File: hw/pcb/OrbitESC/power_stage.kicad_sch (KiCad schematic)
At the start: 0 parts

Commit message: Add power stage components
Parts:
- added C12, C13, C15, C17: 100nF, Capacitor_SMD:C_0402_1005Metric, symbol Device:C
- added C14, C16, C19, C20, C21: 2.2uF, Capacitor_SMD:C_0805_2012Metric, symbol Device:C
- added C18: 10uF, Capacitor_SMD:C_0805_2012Metric, symbol Device:C
- added R21, R22, R23, R25, R28, R29, R30, R31, R34: 10k, Resistor_SMD:R_0402_1005Metric, symbol Device:R_US
- added R24: 1.5k, Resistor_SMD:R_0402_1005Metric, symbol Device:R_US
- added R26, R27, R32, R33, R35, R36: 1k, Resistor_SMD:R_0402_1005Metric, symbol Device:R_US
- added U5: DRV8300DRGER, Package_DFN_QFN:VQFN-24-1EP_4x4mm_P0.5mm_EP2.45x2.45mm_ThermalVias, symbol GateDrivers:DRV8300DRGER
- added U6: TSV994, Package_SO:TSSOP-14_4.4x5mm_P0.65mm, symbol Amplifier_Operational:TSV994
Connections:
- new net: R25.2, R26.2, U6.2 (-)
- new net: R21.1, R22.2, U6.12 (+)
- new net: C21.1, U5.14 (BSTC)
- new net: C20.1, U5.17 (BSTB)
- new net: C19.1, U5.20 (BSTA)
- new net: C14.1, R28.1, U6.13 (-), U6.14
- new net: R33.2, U6.10 (+)
- new net: R31.2, R32.2, U6.9 (-)
- new net: R27.2, U6.3 (+)
- new net: R34.2, R35.2, U6.6 (-)
- new net: R36.2, U6.5 (+)
- new net +3.3V: R29.2
- new net +3.3VADC: C12.2, C16.1, R21.2, U6.4 (V+)
- new net AH: U5.22 (INHA)
- new net AL: U5.1 (INLA)
- new net A_ISENSE_N: R36.1
- new net A_ISENSE_P: R35.1
- new net BH: U5.23 (INHB)
- new net BL: U5.2 (INLB)
- new net B_ISENSE_N: R33.1
- new net B_ISENSE_P: R32.1
- new net CH: U5.24 (INHC)
- new net CL: U5.3 (INLC)
- new net C_ISENSE_N: R27.1
- new net C_ISENSE_P: R26.1
- new net GHA: U5.19 (GHA)
- new net GHB: U5.16 (GHB)
- new net GHC: U5.13 (GHC)
- new net GLA: U5.11 (GLA)
- new net GLB: U5.10 (GLB)
- new net GLC: U5.9 (GLC)
- new net GND: C12.1, C14.2, C16.2, C17.1, C18.2, R22.1, U5.6 (GND), U6.11 (V-)
- new net GNDD: C13.2, C15.2, R24.2, R30.1
- new net IA: R34.1, U6.7
- new net IB: R31.1, U6.8
- new net IC: R25.1, U6.1
- new net ISenseVRef: R28.2
- new net SHA: C19.2, U5.18 (SHA)
- new net SHB: C20.2, U5.15 (SHB)
- new net SHC: C21.2, U5.12 (SHC)
- new net VDC: C17.2, C18.1, R23.2, U5.4 (GVDD)
- new net VL: C15.1, R29.1, R30.2
- new net VS: C13.1, R23.1, R24.1
- no-connect marks 0 -> 2
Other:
- note added: "3PH Drive Temp Sense"
- note added: "Logic Voltage Sense"
- note added: "Motor Terminal Voltage"
- note added: "Supply Voltage Sense"

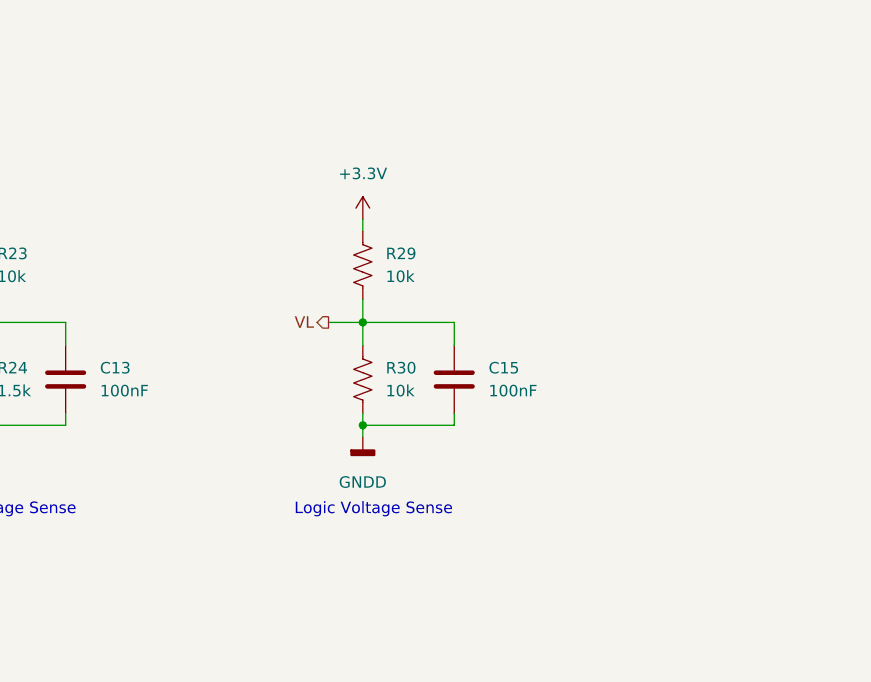
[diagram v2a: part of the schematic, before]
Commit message: Fill out majority of schematic
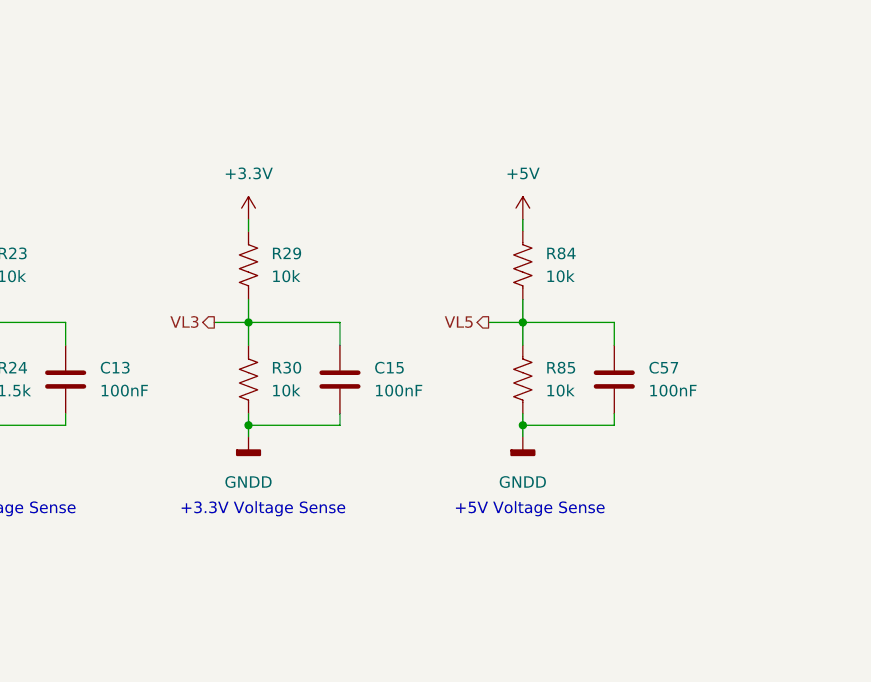
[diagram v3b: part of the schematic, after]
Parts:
- added C57: 100nF, Capacitor_SMD:C_0402_1005Metric, symbol Device:C
- added R84, R85: 10k, Resistor_SMD:R_0402_1005Metric, symbol Device:R_US
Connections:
- net GNDD: now also C57.2, R85.1
- net VL renamed VL3
- new net +5V: R84.2
- new net VL5: C57.1, R84.1, R85.2
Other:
- note added: "+3.3V Voltage Sense"
- note added: "+5V Voltage Sense"
- note removed: "Logic Voltage Sense"
- moved on the sheet: C15, R29, R30

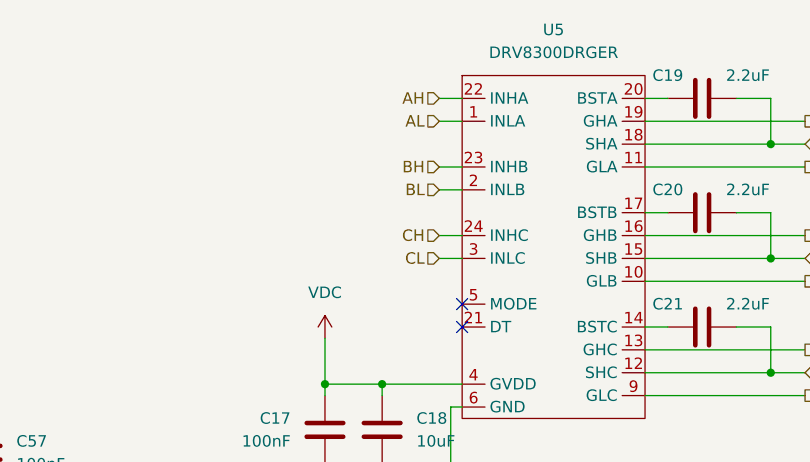
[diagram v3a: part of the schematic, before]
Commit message: Add test pads
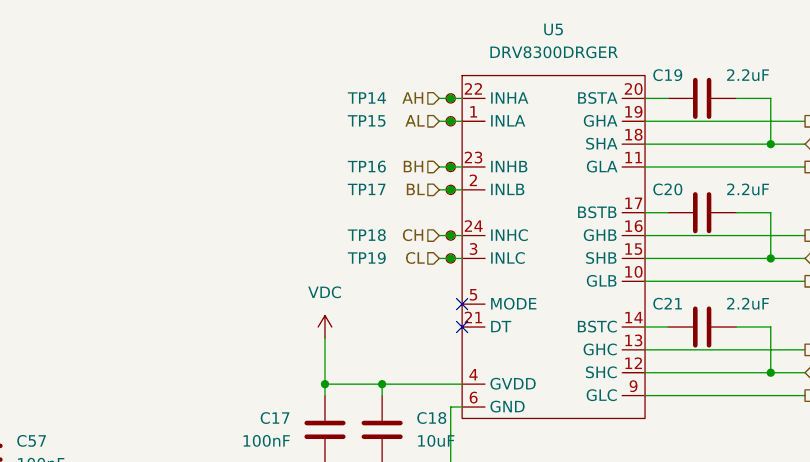
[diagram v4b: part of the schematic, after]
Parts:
- added TP14: AH, TestPoint:TestPoint_Pad_D1.0mm, symbol Connector:TestPoint_Small
- added TP15: AL, TestPoint:TestPoint_Pad_D1.0mm, symbol Connector:TestPoint_Small
- added TP16: BH, TestPoint:TestPoint_Pad_D1.0mm, symbol Connector:TestPoint_Small
- added TP17: BL, TestPoint:TestPoint_Pad_D1.0mm, symbol Connector:TestPoint_Small
- added TP18: CH, TestPoint:TestPoint_Pad_D1.0mm, symbol Connector:TestPoint_Small
- added TP19: CL, TestPoint:TestPoint_Pad_D1.0mm, symbol Connector:TestPoint_Small
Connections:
- net AH: now also TP14.1
- net AL: now also TP15.1
- net BH: now also TP16.1
- net BL: now also TP17.1
- net CH: now also TP18.1
- net CL: now also TP19.1
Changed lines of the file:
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@@
   (junction (at 236.22 48.26) (diameter 0) (color 0 0 0 0)
   )
+  (junction (at 200.66 45.72) (diameter 0) (color 0 0 0 0)
+  )
   (junction (at 151.13 138.43) (diameter 0) (color 0 0 0 0)
   )
+  (junction (at 200.66 58.42) (diameter 0) (color 0 0 0 0)
+  )
   (junction (at 236.22 73.66) (diameter 0) (color 0 0 0 0)
   )
@@
   (junction (at 236.22 60.96) (diameter 0) (color 0 0 0 0)
   )
+  (junction (at 200.66 60.96) (diameter 0) (color 0 0 0 0)
+  )
   (junction (at 134.62 165.186) (diameter 0) (color 0 0 0 0)
   )
@@
   (junction (at 77.47 76.2) (diameter 0) (color 0 0 0 0)
   )
+  (junction (at 200.66 43.18) (diameter 0) (color 0 0 0 0)
+  )
   (junction (at 196.85 140.97) (diameter 0) (color 0 0 0 0)
   )
   (junction (at 186.69 74.93) (diameter 0) (color 0 0 0 0)
+  )
+  (junction (at 200.66 53.34) (diameter 0) (color 0 0 0 0)
+  )
+  (junction (at 200.66 50.8) (diameter 0) (color 0 0 0 0)
   )
   (junction (at 107.95 87.63) (diameter 0) (color 0 0 0 0)
@@
   (no_connect (at 201.93 66.04))
   (no_connect (at 201.93 68.58))
-  (wire (pts (xy 199.39 50.8) (xy 201.93 50.8))
+  (wire (pts (xy 199.39 50.8) (xy 200.66 50.8))
     (stroke (width 0) (type default) (color 0 0 0 0))
   )
@@
     (stroke (width 0) (type default) (color 0 0 0 0))
   )
+  (wire (pts (xy 200.66 58.42) (xy 201.93 58.42))
+    (stroke (width 0) (type default) (color 0 0 0 0))
+  )
   (wire (pts (xy 186.69 74.93) (xy 186.69 76.2))
     (stroke (width 0) (type default) (color 0 0 0 0))
   )
-  (wire (pts (xy 199.39 45.72) (xy 201.93 45.72))
+  (wire (pts (xy 199.39 45.72) (xy 200.66 45.72))
+    (stroke (width 0) (type default) (color 0 0 0 0))
+  )
+  (wire (pts (xy 200.66 50.8) (xy 201.93 50.8))
     (stroke (width 0) (type default) (color 0 0 0 0))
   )
@@
     (stroke (width 0) (type default) (color 0 0 0 0))
   )
+  (wire (pts (xy 200.66 45.72) (xy 201.93 45.72))
+    (stroke (width 0) (type default) (color 0 0 0 0))
+  )
   (wire (pts (xy 236.22 73.66) (xy 240.03 73.66))
     (stroke (width 0) (type default) (color 0 0 0 0))
@@
     (stroke (width 0) (type default) (color 0 0 0 0))
   )
+  (wire (pts (xy 200.66 43.18) (xy 201.93 43.18))
+    (stroke (width 0) (type default) (color 0 0 0 0))
+  )
   (wire (pts (xy 86.36 174.076) (xy 88.9 174.076))
     (stroke (width 0) (type default) (color 0 0 0 0))
@@
     (stroke (width 0) (type default) (color 0 0 0 0))
   )
-  (wire (pts (xy 199.39 58.42) (xy 201.93 58.42))
+  (wire (pts (xy 199.39 58.42) (xy 200.66 58.42))
     (stroke (width 0) (type default) (color 0 0 0 0))
   )
@@
     (stroke (width 0) (type default) (color 0 0 0 0))
   )
-  (wire (pts (xy 199.39 43.18) (xy 201.93 43.18))
+  (wire (pts (xy 199.39 43.18) (xy 200.66 43.18))
     (stroke (width 0) (type default) (color 0 0 0 0))
   )
@@
     (stroke (width 0) (type default) (color 0 0 0 0))
   )
+  (wire (pts (xy 200.66 60.96) (xy 201.93 60.96))
+    (stroke (width 0) (type default) (color 0 0 0 0))
+  )
   (wire (pts (xy 186.69 74.93) (xy 193.04 74.93))
     (stroke (width 0) (type default) (color 0 0 0 0))
@@
     (stroke (width 0) (type default) (color 0 0 0 0))
   )
+  (wire (pts (xy 200.66 53.34) (xy 201.93 53.34))
+    (stroke (width 0) (type default) (color 0 0 0 0))
+  )
   (wire (pts (xy 133.35 128.27) (xy 133.35 140.97))
     (stroke (width 0) (type default) (color 0 0 0 0))
@@
     (stroke (width 0) (type default) (color 0 0 0 0))
   )
-  (wire (pts (xy 199.39 60.96) (xy 201.93 60.96))
+  (wire (pts (xy 199.39 60.96) (xy 200.66 60.96))
     (stroke (width 0) (type default) (color 0 0 0 0))
   )
@@
     (stroke (width 0) (type default) (color 0 0 0 0))
   )
-  (wire (pts (xy 199.39 53.34) (xy 201.93 53.34))
+  (wire (pts (xy 199.39 53.34) (xy 200.66 53.34))
     (stroke (width 0) (type default) (color 0 0 0 0))
   )
@@
     )
     (property "Datasheet" "" (id 3) (at 107.95 88.9 0)
+      (effects (font (size 1.27 1.27)) hide)
+    )
+    (pin "1")
+  )
+  (symbol (lib_id "Connector:TestPoint_Small") (at 200.66 43.18 0) (unit 1)
+    (in_bom yes) (on_board yes)
+    (property "Reference" "TP14" (id 0) (at 189.23 43.18 0)
+      (effects (font (size 1.27 1.27)) (justify left))
+    )
+    (property "Value" "AH" (id 1) (at 202.565 44.4499 0)
+      (effects (font (size 1.27 1.27)) (justify left) hide)
+    )
+    (property "Footprint" "TestPoint:TestPoint_Pad_D1.0mm" (id 2) (at 205.74 43.18 0)
+      (effects (font (size 1.27 1.27)) hide)
+    )
+    (property "Datasheet" "~" (id 3) (at 205.74 43.18 0)
       (effects (font (size 1.27 1.27)) hide)
     )
@@
     (pin "2")
   )
+  (symbol (lib_id "Connector:TestPoint_Small") (at 200.66 53.34 0) (unit 1)
+    (in_bom yes) (on_board yes)
+    (property "Reference" "TP17" (id 0) (at 189.23 53.34 0)
+      (effects (font (size 1.27 1.27)) (justify left))
+    )
+    (property "Value" "BL" (id 1) (at 202.565 54.6099 0)
+      (effects (font (size 1.27 1.27)) (justify left) hide)
+    )
+    (property "Footprint" "TestPoint:TestPoint_Pad_D1.0mm" (id 2) (at 205.74 53.34 0)
+      (effects (font (size 1.27 1.27)) hide)
+    )
+    (property "Datasheet" "~" (id 3) (at 205.74 53.34 0)
+      (effects (font (size 1.27 1.27)) hide)
+    )
+    (pin "1")
+  )
   (symbol (lib_id "power:GND") (at 186.69 85.09 0) (unit 1)
     (in_bom yes) (on_board yes) (fields_autoplaced)
@@
     )
     (property "Datasheet" "" (id 3) (at 60.96 163.916 0)
+      (effects (font (size 1.27 1.27)) hide)
+    )
+    (pin "1")
+  )
+  (symbol (lib_id "Connector:TestPoint_Small") (at 200.66 50.8 0) (unit 1)
+    (in_bom yes) (on_board yes)
+    (property "Reference" "TP16" (id 0) (at 189.23 50.8 0)
+      (effects (font (size 1.27 1.27)) (justify left))
+    )
+    (property "Value" "BH" (id 1) (at 202.565 52.0699 0)
+      (effects (font (size 1.27 1.27)) (justify left) hide)
+    )
+    (property "Footprint" "TestPoint:TestPoint_Pad_D1.0mm" (id 2) (at 205.74 50.8 0)
+      (effects (font (size 1.27 1.27)) hide)
+    )
+    (property "Datasheet" "~" (id 3) (at 205.74 50.8 0)
       (effects (font (size 1.27 1.27)) hide)
     )
@@
     (pin "1")
     (pin "2")
+  )
+  (symbol (lib_id "Connector:TestPoint_Small") (at 200.66 58.42 0) (unit 1)
+    (in_bom yes) (on_board yes)
+    (property "Reference" "TP18" (id 0) (at 189.23 58.42 0)
+      (effects (font (size 1.27 1.27)) (justify left))
+    )
+    (property "Value" "CH" (id 1) (at 201.803 60.1222 0)
+      (effects (font (size 1.27 1.27)) (justify left) hide)
+    )
+    (property "Footprint" "TestPoint:TestPoint_Pad_D1.0mm" (id 2) (at 205.74 58.42 0)
+      (effects (font (size 1.27 1.27)) hide)
+    )
+    (property "Datasheet" "~" (id 3) (at 205.74 58.42 0)
+      (effects (font (size 1.27 1.27)) hide)
+    )
+    (pin "1")
   )
   (symbol (lib_id "Device:C") (at 193.04 80.01 0) (unit 1)
@@
     (pin "4")
   )
+  (symbol (lib_id "Connector:TestPoint_Small") (at 200.66 45.72 0) (unit 1)
+    (in_bom yes) (on_board yes)
+    (property "Reference" "TP15" (id 0) (at 189.23 45.72 0)
+      (effects (font (size 1.27 1.27)) (justify left))
+    )
+    (property "Value" "AL" (id 1) (at 202.565 46.9899 0)
+      (effects (font (size 1.27 1.27)) (justify left) hide)
+    )
+    (property "Footprint" "TestPoint:TestPoint_Pad_D1.0mm" (id 2) (at 205.74 45.72 0)
+      (effects (font (size 1.27 1.27)) hide)
+    )
+    (property "Datasheet" "~" (id 3) (at 205.74 45.72 0)
+      (effects (font (size 1.27 1.27)) hide)
+    )
+    (pin "1")
+  )
   (symbol (lib_id "Amplifier_Operational:TSV994") (at 78.74 174.076 0) (mirror x) (unit 4)
     (in_bom yes) (on_board yes) (fields_autoplaced)
@@
     (pin "2")
   )
+  (symbol (lib_id "Connector:TestPoint_Small") (at 200.66 60.96 0) (unit 1)
+    (in_bom yes) (on_board yes)
+    (property "Reference" "TP19" (id 0) (at 189.23 60.96 0)
+      (effects (font (size 1.27 1.27)) (justify left))
+    )
+    (property "Value" "CL" (id 1) (at 202.565 62.2299 0)
+      (effects (font (size 1.27 1.27)) (justify left) hide)
+    )
+    (property "Footprint" "TestPoint:TestPoint_Pad_D1.0mm" (id 2) (at 205.74 60.96 0)
+      (effects (font (size 1.27 1.27)) hide)
+    )
+    (property "Datasheet" "~" (id 3) (at 205.74 60.96 0)
+      (effects (font (size 1.27 1.27)) hide)
+    )
+    (pin "1")
+  )
   (symbol (lib_id "Device:C") (at 228.6 43.18 90) (unit 1)

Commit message: Schematic checklist runthrough
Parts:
- U5: DigiKey (none) -> 296-DRV8300DRGERCT-ND
- U6: DigiKey (none) -> 497-6003-1-ND
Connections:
- net ISenseVRef: now also R27.2, R33.2, R36.2, U6.10 (+), U6.3 (+), U6.5 (+)
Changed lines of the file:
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@@
   (junction (at 200.66 60.96) (diameter 0) (color 0 0 0 0)
   )
+  (junction (at 87.63 143.51) (diameter 0) (color 0 0 0 0)
+  )
+  (junction (at 214.63 143.51) (diameter 0) (color 0 0 0 0)
+  )
   (junction (at 134.62 165.186) (diameter 0) (color 0 0 0 0)
   )
@@
   )
   (junction (at 200.66 53.34) (diameter 0) (color 0 0 0 0)
+  )
+  (junction (at 151.13 143.51) (diameter 0) (color 0 0 0 0)
   )
   (junction (at 200.66 50.8) (diameter 0) (color 0 0 0 0)
@@
     (stroke (width 0) (type default) (color 0 0 0 0))
   )
+  (wire (pts (xy 214.63 143.51) (xy 215.9 143.51))
+    (stroke (width 0) (type default) (color 0 0 0 0))
+  )
   (wire (pts (xy 77.47 73.66) (xy 77.47 76.2))
     (stroke (width 0) (type default) (color 0 0 0 0))
@@
     (stroke (width 0) (type default) (color 0 0 0 0))
   )
+  (wire (pts (xy 214.63 143.51) (xy 214.63 144.78))
+    (stroke (width 0) (type default) (color 0 0 0 0))
+  )
   (wire (pts (xy 196.85 128.27) (xy 196.85 140.97))
     (stroke (width 0) (type default) (color 0 0 0 0))
@@
     (stroke (width 0) (type default) (color 0 0 0 0))
   )
-  (wire (pts (xy 213.36 143.51) (xy 215.9 143.51))
+  (wire (pts (xy 213.36 143.51) (xy 214.63 143.51))
     (stroke (width 0) (type default) (color 0 0 0 0))
   )
@@
     (stroke (width 0) (type default) (color 0 0 0 0))
   )
+  (wire (pts (xy 87.63 143.51) (xy 88.9 143.51))
+    (stroke (width 0) (type default) (color 0 0 0 0))
+  )
   (wire (pts (xy 77.47 76.2) (xy 77.47 78.74))
     (stroke (width 0) (type default) (color 0 0 0 0))
@@
     (stroke (width 0) (type default) (color 0 0 0 0))
   )
-  (wire (pts (xy 86.36 143.51) (xy 88.9 143.51))
+  (wire (pts (xy 86.36 143.51) (xy 87.63 143.51))
     (stroke (width 0) (type default) (color 0 0 0 0))
   )
@@
     (stroke (width 0) (type default) (color 0 0 0 0))
   )
+  (wire (pts (xy 151.13 143.51) (xy 152.4 143.51))
+    (stroke (width 0) (type default) (color 0 0 0 0))
+  )
   (wire (pts (xy 223.52 143.51) (xy 226.06 143.51))
     (stroke (width 0) (type default) (color 0 0 0 0))
@@
     (stroke (width 0) (type default) (color 0 0 0 0))
   )
-  (wire (pts (xy 149.86 143.51) (xy 152.4 143.51))
+  (wire (pts (xy 149.86 143.51) (xy 151.13 143.51))
     (stroke (width 0) (type default) (color 0 0 0 0))
   )
@@
     (stroke (width 0) (type default) (color 0 0 0 0))
   )
+  (wire (pts (xy 87.63 143.51) (xy 87.63 144.78))
+    (stroke (width 0) (type default) (color 0 0 0 0))
+  )
   (wire (pts (xy 118.11 87.63) (xy 118.11 86.36))
     (stroke (width 0) (type default) (color 0 0 0 0))
@@
   )
   (wire (pts (xy 36.83 90.17) (xy 44.45 90.17))
+    (stroke (width 0) (type default) (color 0 0 0 0))
+  )
+  (wire (pts (xy 151.13 143.51) (xy 151.13 144.78))
     (stroke (width 0) (type default) (color 0 0 0 0))
   )
@@
     (effects (font (size 1.27 1.27)) (justify left bottom))
   )
+  (global_label "ISenseVRef" (shape passive) (at 87.63 144.78 270) (fields_autoplaced)
+    (effects (font (size 1.27 1.27)) (justify right))
+    (property "Intersheet References" "${INTERSHEET_REFS}" (id 0) (at 87.7094 157.5345 90)
+      (effects (font (size 1.27 1.27)) (justify right) hide)
+    )
+  )
+  (global_label "ISenseVRef" (shape passive) (at 214.63 144.78 270) (fields_autoplaced)
+    (effects (font (size 1.27 1.27)) (justify right))
+    (property "Intersheet References" "${INTERSHEET_REFS}" (id 0) (at 214.7094 157.5345 90)
+      (effects (font (size 1.27 1.27)) (justify right) hide)
+    )
+  )
   (global_label "ISenseVRef" (shape passive) (at 102.87 174.076 0) (fields_autoplaced)
     (effects (font (size 1.27 1.27)) (justify left))
     (property "Intersheet References" "${INTERSHEET_REFS}" (id 0) (at 115.6245 173.9966 0)
       (effects (font (size 1.27 1.27)) (justify left) hide)
+    )
+  )
+  (global_label "ISenseVRef" (shape passive) (at 151.13 144.78 270) (fields_autoplaced)
+    (effects (font (size 1.27 1.27)) (justify right))
+    (property "Intersheet References" "${INTERSHEET_REFS}" (id 0) (at 151.2094 157.5345 90)
+      (effects (font (size 1.27 1.27)) (justify right) hide)
     )
   )
@@
     )
     (property "Datasheet" "https://www.ti.com/lit/ds/symlink/drv8300.pdf?HQS=dis-dk-null-digikeymode-dsf-pf-null-wwe&ts=1661717575056" (id 3) (at 209.55 53.34 0)
+      (effects (font (size 1.27 1.27)) hide)
+    )
+    (property "DigiKey" "296-DRV8300DRGERCT-ND" (id 4) (at 212.09 59.69 0)
       (effects (font (size 1.27 1.27)) hide)
     )
@@
     )
     (property "Datasheet" "https://www.st.com/resource/en/datasheet/tsv994.pdf" (id 3) (at 140.97 146.05 0)
+      (effects (font (size 1.27 1.27)) hide)
+    )
+    (property "DigiKey" "497-6003-1-ND" (id 4) (at 142.24 140.97 0)
       (effects (font (size 1.27 1.27)) hide)
     )
@@
       (effects (font (size 1.27 1.27)) hide)
     )
+    (property "DigiKey" "497-6003-1-ND" (id 4) (at 142.24 140.97 0)
+      (effects (font (size 1.27 1.27)) hide)
+    )
     (pin "1")
     (pin "2")
@@
       (effects (font (size 1.27 1.27)) hide)
     )
+    (property "DigiKey" "497-6003-1-ND" (id 4) (at 142.24 140.97 0)
+      (effects (font (size 1.27 1.27)) hide)
+    )
     (pin "1")
     (pin "2")
@@
       (effects (font (size 1.27 1.27)) hide)
     )
+    (property "DigiKey" "497-6003-1-ND" (id 4) (at 142.24 140.97 0)
+      (effects (font (size 1.27 1.27)) hide)
+    )
     (pin "1")
     (pin "2")
@@
       (effects (font (size 1.27 1.27)) hide)
     )
+    (property "DigiKey" "497-6003-1-ND" (id 4) (at 142.24 140.97 0)
+      (effects (font (size 1.27 1.27)) hide)
+    )
